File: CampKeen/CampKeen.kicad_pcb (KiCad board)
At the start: 4 copper layers, 177.8 x 142.2 mm, 279 parts, among them IC1 CD74HC4050ME4, IC2 LM2597MX-ADJ_NOPB, IC3 LM2670SX-5.0_NOPB, IC4 DS3231SN#, IC5 OPA2340PA, IC6 OPA2340PA, J1 Vin, J2 Screw_Terminal_01x03, J3 CircuitSetupsSplitPhase, J4 Conn_01x02, J5 Conn_01x02, J6 Conn_01x02, J7 GenEnclosure, J8 GenHeadL, J9 GenHeadR, P1 Power, P10 CONN_01X01, P11 CONN_01X01, P12 CONN_01X01, P13 CONN_01X01, P2 Analog, P3 Analog, P4 Digital, P5 PWM, P6 PWM, P7 Communication, P8 CONN_01X01, P9 CONN_01X01, Q1 IRF9Z34NPBF, Q10 2N7000, Q11 IRF9Z34NPBF, Q12 2N7000, Q13 2N7000, Q14 2N7000, Q15 2N7000, Q16 2N7000, Q17 2N7000, Q18 2N7000, Q19 2N7000, Q2 2N7000, Q20 2N7000, Q21 2N7000, Q22 2N7000, Q23 2N7000, Q24 2N7000, Q25 2N7000, Q26 2N7000, Q27 2N7000, Q28 2N7000, Q29 2N7000, Q3 IRF9Z34NPBF, Q30 2N7000, Q31 2N7000, Q32 IRF9Z34NPBF, Q33 IRF9Z34NPBF, Q34 2N7000, Q35 IRF9Z34NPBF, Q36 2N7000, Q37 IRF9Z34NPBF, Q38 2N7000, Q39 IRF9Z34NPBF, Q4 2N7000, Q40 2N7000, Q41 IRF9Z34NPBF, Q42 2N7000, Q43 2N7000, Q44 IRF9Z34NPBF, Q45 IRF9Z34NPBF, Q46 2N7000, Q47 IRF9Z34NPBF, Q48 2N7000, Q49 IRF9Z34NPBF, Q5 2N7000, Q50 2N7000, Q51 IRF9Z34NPBF, Q52 2N7000, Q53 IRF9Z34NPBF, Q54 2N7000, Q55 IRF9Z34NPBF, Q56 2N7000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

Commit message: some annotation.
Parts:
- removed R117, R120: 10k, Resistor_THT:R_Axial_DIN0207_L6.3mm_D2.5mm_P2.54mm_Vertical
- removed Tanks1, Tanks2: TanksVS, SamacSys_Parts:BK_HTC-15M
- removed Z16, Z17: BZX79C10, SamacSys_Parts:DIOAD1068W53L380D172
- added D4: SR305-TP, SamacSys_Parts:DIOAD2860W130L840D505, F.Cu at (-17.8, -85.2)
- added D5: SR305-TP, SamacSys_Parts:DIOAD2860W130L840D505, F.Cu at (-17.8, -78.3)
- moved Z4 201.9 mm to (-4.99, -48.4)
- moved R81 198.4 mm to (13.5, -25.2)
- moved R112 197.5 mm to (85.7, -66.8)
- moved Q30 190.1 mm to (21.1, -44.5)
- moved R30 188.7 mm to (126.9, -29.9)
- moved Q32 188.5 mm to (10.6, -43.4)
- moved R113 184.6 mm to (85.7, -62.8)
- moved R31 183.6 mm to (120.8, -25.9)
- moved R27 183.0 mm to (126.9, -25.9)
- moved R50 179.8 mm to (61.1, -4.28)
- moved R79 178.8 mm to (25.8, -31.9)
- moved R26 178.2 mm to (126.9, -21.8)
- moved R29 178.2 mm to (120.8, -21.8)
- moved R28 176.1 mm to (114.6, -29.9)
- moved R82 172.2 mm to (25.8, -35.9)
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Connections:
- 5VOut1 pad 1: +5V -> Net-(5VOut1-Pad1)
- 5VOut1 pad 2: Net-(5VOut1-Pad2) -> +5V
- C10 pad 1: +5V -> Net-(5VOut1-Pad1)
- IC3 pad 6: +5V -> Net-(5VOut1-Pad1)
- IO2 pad 1: Net-(5VOut1-Pad2) -> +5V
- J2 pad 1: +12V -> Net-(D4-Pad1)
- L1 pad 2: +5V -> Net-(5VOut1-Pad1)
- Q11 pad 3: Net-(Q11-Pad3) -> +BATT
- Q16 pad 3: +5V -> +5VL
- Q17 pad 3: +5V -> +5VL
- Q18 pad 3: +5V -> +5VL
- Q19 pad 3: +5V -> +5VL
- Q20 pad 3: +5V -> +5VL
- Q21 pad 3: +5V -> +5VL
- Q22 pad 3: +5V -> +5VL
- Q23 pad 3: +5V -> +5VL
- Q24 pad 3: +5V -> +5VL
- Q25 pad 3: +5V -> +5VL
- Q26 pad 3: +5V -> +5VL
- Q27 pad 3: +5V -> +5VL
- Q28 pad 3: +5V -> +5VL
- Q29 pad 3: +5V -> +5VL
- Q3 pad 3: Net-(Q3-Pad3) -> +BATT
- Q55 pad 1: Net-(Q55-Pad1) -> Net-(Q54-Pad3)
- Q57 pad 1: Net-(Q57-Pad1) -> Net-(Q56-Pad3)
- R116 pad 2: Net-(Q55-Pad1) -> Net-(Q54-Pad3)
- R119 pad 2: Net-(Q57-Pad1) -> Net-(Q56-Pad3)
- R16 pad 1: Net-(Q3-Pad3) -> +BATT
- R41 pad 1: Net-(Q11-Pad3) -> +BATT
- Z1 pad 1: Net-(Q3-Pad3) -> +BATT
- Z3 pad 1: Net-(Q11-Pad3) -> +BATT
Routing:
- net Net-(D2-Pad1): track 20.6 -> 5.43 mm
- net Net-(5VOut1-Pad1): track 0.00 -> 13.9 mm
- net +5V: track 14.0 -> 0.10 mm

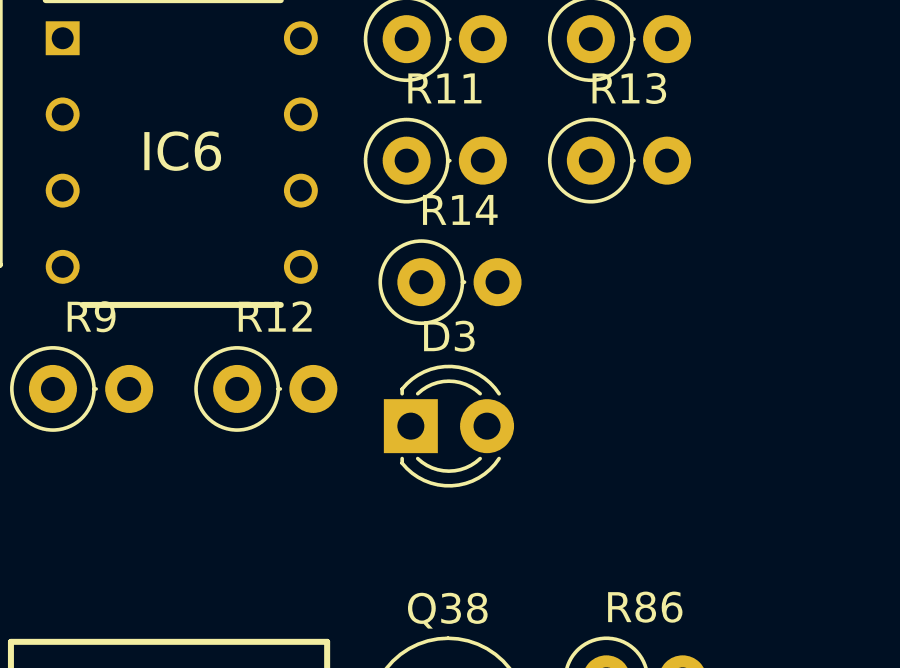
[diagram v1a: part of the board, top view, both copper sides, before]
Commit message: added ACEMON on boot and Waterpumpsense on boot commands. Autoformat
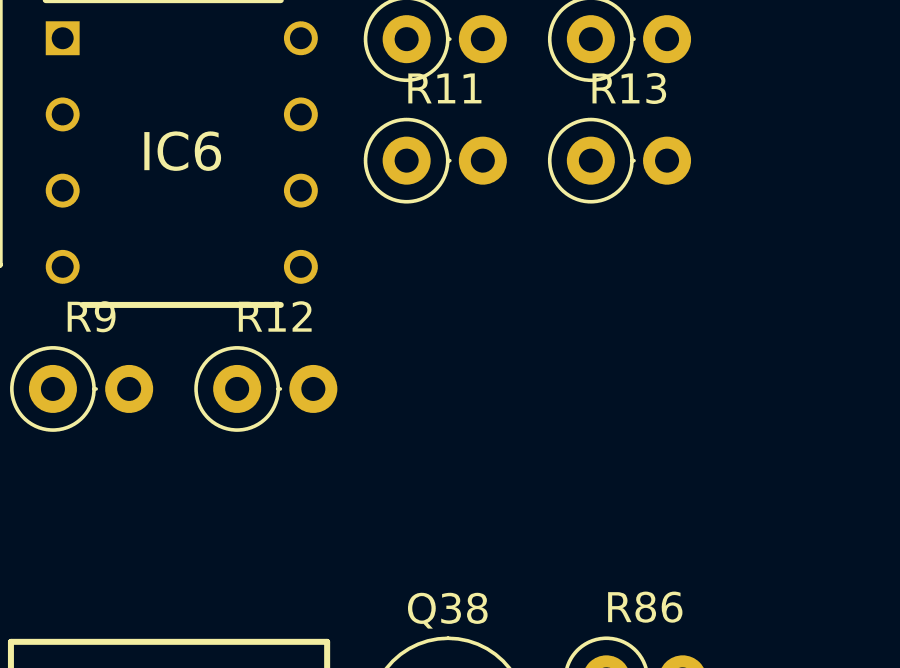
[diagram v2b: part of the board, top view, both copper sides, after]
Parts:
- removed D3: LED, LED_THT:LED_D3.0mm
- removed R14: 330, Resistor_THT:R_Axial_DIN0207_L6.3mm_D2.5mm_P2.54mm_Vertical
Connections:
- P5 pad 5: DisplayLED -> (no net)

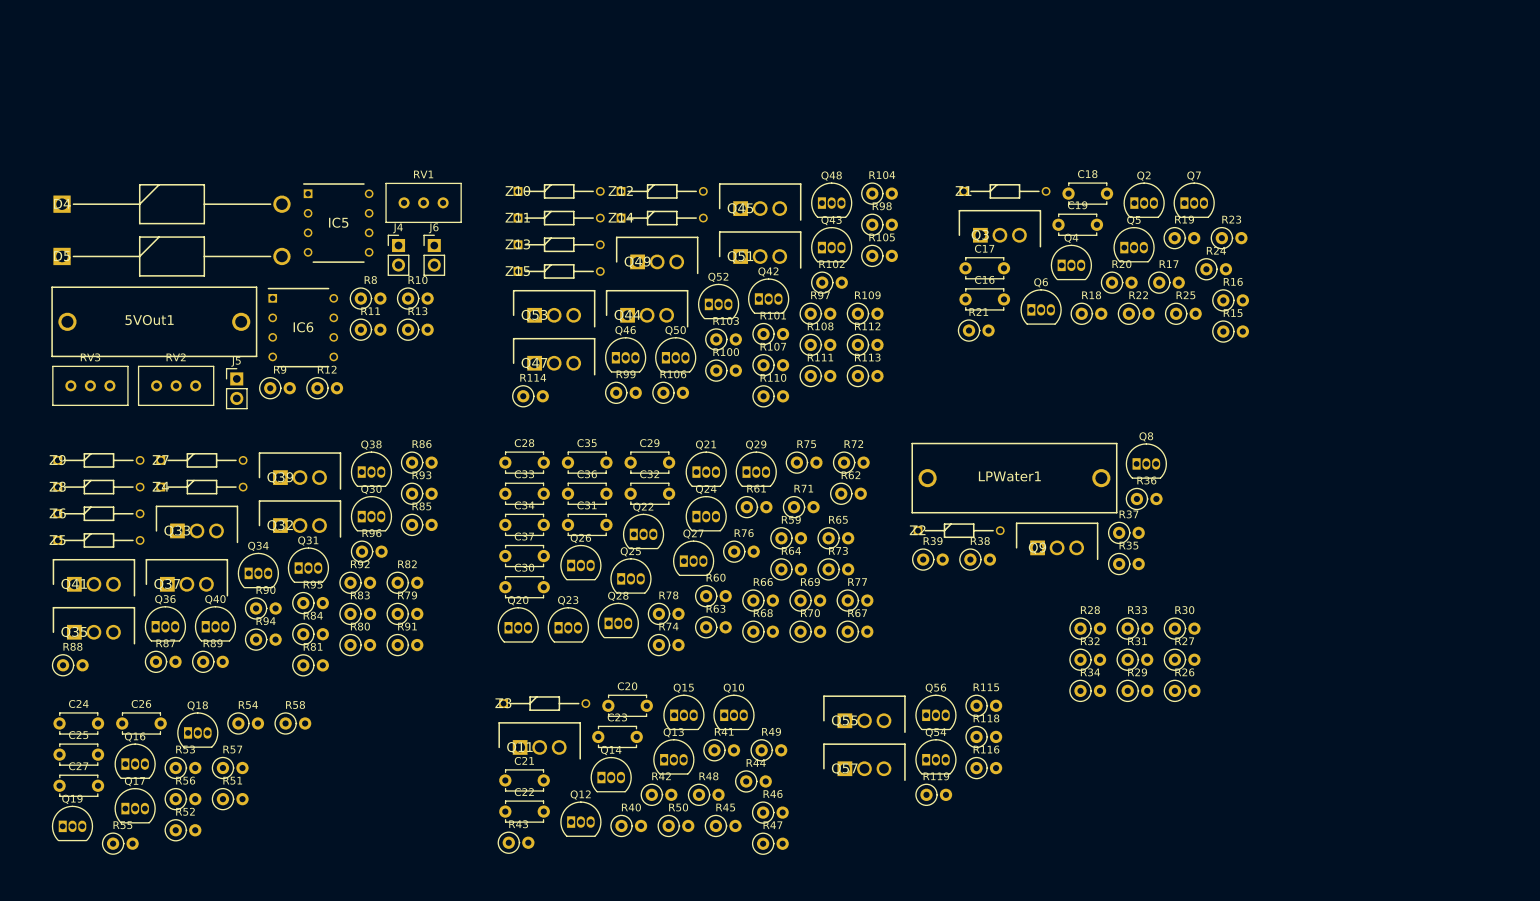
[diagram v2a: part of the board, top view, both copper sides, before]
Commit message: schematic done for Input isolation updates.
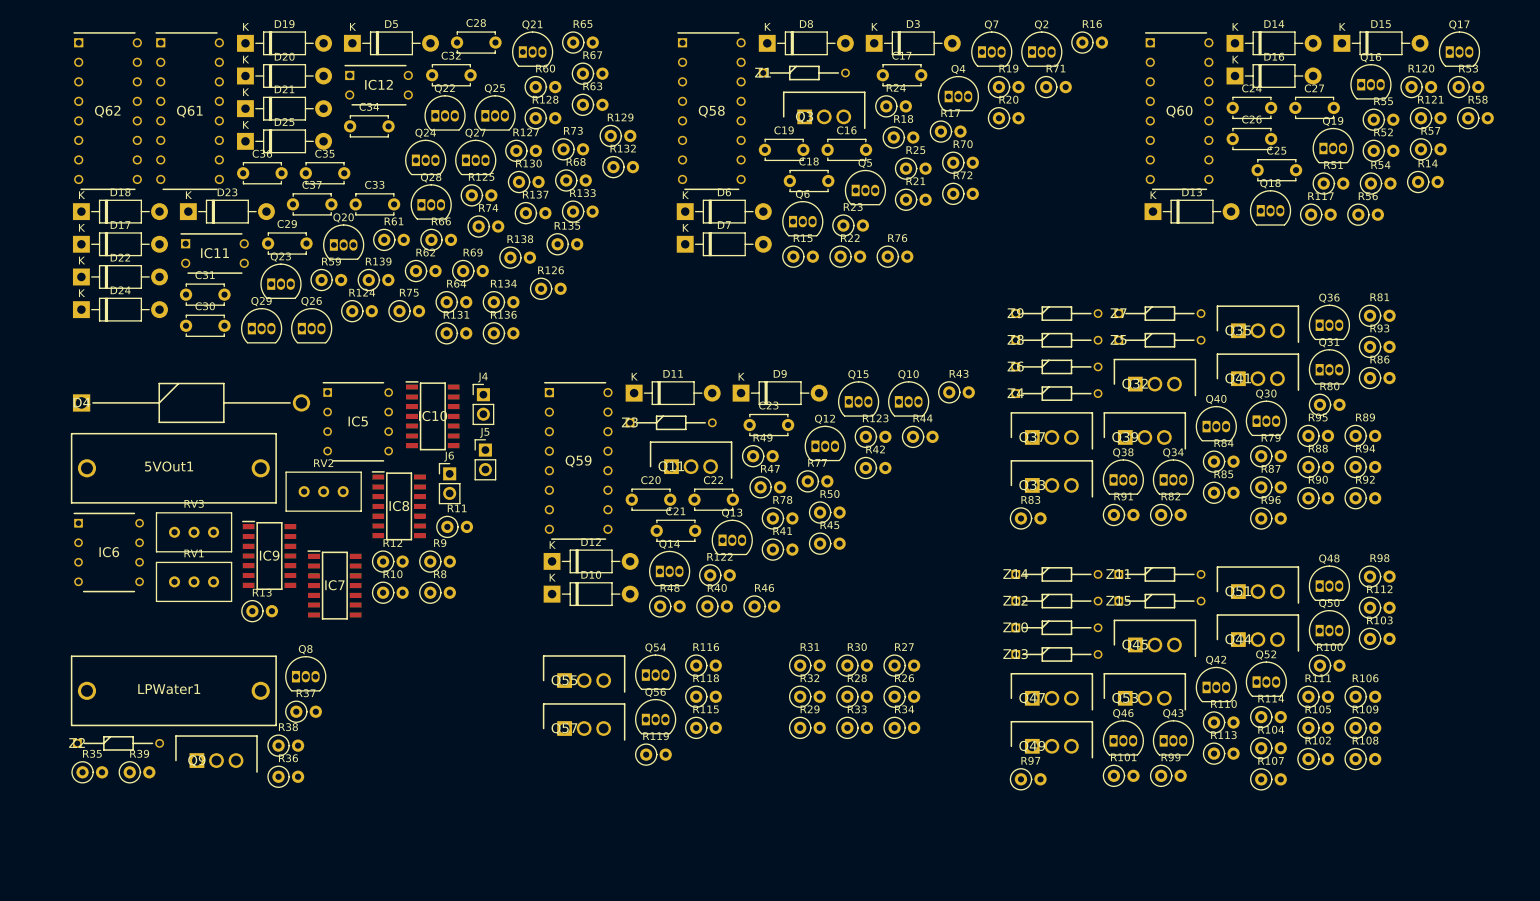
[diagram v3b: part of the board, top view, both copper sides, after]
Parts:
- added D10: 1N4007, Diode_THT:D_DO-41_SOD81_P10.16mm_Horizontal, F.Cu at (45.9, -34.4)
- added D11: 1N4007, Diode_THT:D_DO-41_SOD81_P10.16mm_Horizontal, F.Cu at (56.6, -60.6)
- added D12: 1N4007, Diode_THT:D_DO-41_SOD81_P10.16mm_Horizontal, F.Cu at (45.9, -38.7)
- added D13: 1N4007, Diode_THT:D_DO-41_SOD81_P10.16mm_Horizontal, F.Cu at (124.1, -84.2)
- added D14: 1N4007, Diode_THT:D_DO-41_SOD81_P10.16mm_Horizontal, F.Cu at (134.7, -106.1)
- added D15: 1N4007, Diode_THT:D_DO-41_SOD81_P10.16mm_Horizontal, F.Cu at (148.6, -106.1)
- added D16: 1N4007, Diode_THT:D_DO-41_SOD81_P10.16mm_Horizontal, F.Cu at (134.7, -101.8)
- added D17: 1N4007, Diode_THT:D_DO-41_SOD81_P10.16mm_Horizontal, F.Cu at (-15.3, -79.9)
- added D18: 1N4007, Diode_THT:D_DO-41_SOD81_P10.16mm_Horizontal, F.Cu at (-15.3, -84.2)
- added D19: 1N4007, Diode_THT:D_DO-41_SOD81_P10.16mm_Horizontal, F.Cu at (6.01, -106.1)
- added D20: 1N4007, Diode_THT:D_DO-41_SOD81_P10.16mm_Horizontal, F.Cu at (6.01, -101.8)
- added D21: 1N4007, Diode_THT:D_DO-41_SOD81_P10.16mm_Horizontal, F.Cu at (6.01, -97.6)
- added D22: 1N4007, Diode_THT:D_DO-41_SOD81_P10.16mm_Horizontal, F.Cu at (-15.3, -75.7)
- added D23: 1N4007, Diode_THT:D_DO-41_SOD81_P10.16mm_Horizontal, F.Cu at (-1.42, -84.2)
- added D24: 1N4007, Diode_THT:D_DO-41_SOD81_P10.16mm_Horizontal, F.Cu at (-15.3, -71.4)
- added D25: 1N4007, Diode_THT:D_DO-41_SOD81_P10.16mm_Horizontal, F.Cu at (6.01, -93.3)
- added D3: 1N4007, Diode_THT:D_DO-41_SOD81_P10.16mm_Horizontal, F.Cu at (87.8, -106.1)
- added D6: 1N4007, Diode_THT:D_DO-41_SOD81_P10.16mm_Horizontal, F.Cu at (63.2, -84.2)
- added D7: 1N4007, Diode_THT:D_DO-41_SOD81_P10.16mm_Horizontal, F.Cu at (63.2, -79.9)
- added D8: 1N4007, Diode_THT:D_DO-41_SOD81_P10.16mm_Horizontal, F.Cu at (73.9, -106.1)
- added D9: 1N4007, Diode_THT:D_DO-41_SOD81_P10.16mm_Horizontal, F.Cu at (70.5, -60.6)
- added IC10: SN7404DR, SamacSys_Parts:SOIC127P600X175-14N, F.Cu at (30.4, -57.5)
- added IC11: LTV-814, SamacSys_Parts:DIP762W60P254L460H450Q4N, F.Cu at (2.04, -78.7)
- added IC12: LTV-814, SamacSys_Parts:DIP762W60P254L460H450Q4N, F.Cu at (23.4, -100.6)
- added IC7: SN7404DR, SamacSys_Parts:SOIC127P600X175-14N, F.Cu at (17.6, -35.5)
- added IC8: SN7404DR, SamacSys_Parts:SOIC127P600X175-14N, F.Cu at (26.0, -45.8)
- added IC9: SN7404DR, SamacSys_Parts:SOIC127P600X175-14N, F.Cu at (9.14, -39.4)
- added Q58: LTV-847, SamacSys_Parts:DIP762W60P254L1984H450Q16N, F.Cu at (66.7, -97.3)
- added Q59: LTV-847, SamacSys_Parts:DIP762W60P254L1984H450Q16N, F.Cu at (49.4, -51.8)
- added Q60: LTV-847, SamacSys_Parts:DIP762W60P254L1984H450Q16N, F.Cu at (127.5, -97.3)
- added Q61: LTV-847, SamacSys_Parts:DIP762W60P254L1984H450Q16N, F.Cu at (-1.20, -97.3)
- added Q62: LTV-847, SamacSys_Parts:DIP762W60P254L1984H450Q16N, F.Cu at (-11.9, -97.3)
- added R117: 330, Resistor_THT:R_Axial_DIN0207_L6.3mm_D2.5mm_P2.54mm_Vertical, F.Cu at (144.6, -83.8)
- added R120: 330, Resistor_THT:R_Axial_DIN0207_L6.3mm_D2.5mm_P2.54mm_Vertical, F.Cu at (157.7, -100.4)
- added R121: 330, Resistor_THT:R_Axial_DIN0207_L6.3mm_D2.5mm_P2.54mm_Vertical, F.Cu at (158.9, -96.3)
- added R122: 22k, Resistor_THT:R_Axial_DIN0207_L6.3mm_D2.5mm_P2.54mm_Vertical, F.Cu at (66.5, -36.9)
- added R123: 22k, Resistor_THT:R_Axial_DIN0207_L6.3mm_D2.5mm_P2.54mm_Vertical, F.Cu at (86.7, -54.9)
- added R124: 330, Resistor_THT:R_Axial_DIN0207_L6.3mm_D2.5mm_P2.54mm_Vertical, F.Cu at (19.9, -71.2)
- added R125: 22k, Resistor_THT:R_Axial_DIN0207_L6.3mm_D2.5mm_P2.54mm_Vertical, F.Cu at (35.5, -86.3)
- added R126: 330, Resistor_THT:R_Axial_DIN0207_L6.3mm_D2.5mm_P2.54mm_Vertical, F.Cu at (44.5, -74.1)
- added R127: 22k, Resistor_THT:R_Axial_DIN0207_L6.3mm_D2.5mm_P2.54mm_Vertical, F.Cu at (41.2, -92.1)
- added R128: 22k, Resistor_THT:R_Axial_DIN0207_L6.3mm_D2.5mm_P2.54mm_Vertical, F.Cu at (43.8, -96.3)
- added R129: 22k, Resistor_THT:R_Axial_DIN0207_L6.3mm_D2.5mm_P2.54mm_Vertical, F.Cu at (53.5, -94.0)
- added R130: 22k, Resistor_THT:R_Axial_DIN0207_L6.3mm_D2.5mm_P2.54mm_Vertical, F.Cu at (41.6, -88.0)
- added R131: 22k, Resistor_THT:R_Axial_DIN0207_L6.3mm_D2.5mm_P2.54mm_Vertical, F.Cu at (32.2, -68.4)
- added R132: 330, Resistor_THT:R_Axial_DIN0207_L6.3mm_D2.5mm_P2.54mm_Vertical, F.Cu at (53.9, -90.0)
- added R133: 300, Resistor_THT:R_Axial_DIN0207_L6.3mm_D2.5mm_P2.54mm_Vertical, F.Cu at (48.6, -84.2)
- added R134: 330, Resistor_THT:R_Axial_DIN0207_L6.3mm_D2.5mm_P2.54mm_Vertical, F.Cu at (38.3, -72.4)
- added R135: 330, Resistor_THT:R_Axial_DIN0207_L6.3mm_D2.5mm_P2.54mm_Vertical, F.Cu at (46.6, -79.9)
- added R136: 22k, Resistor_THT:R_Axial_DIN0207_L6.3mm_D2.5mm_P2.54mm_Vertical, F.Cu at (38.3, -68.4)
- added R137: 22k, Resistor_THT:R_Axial_DIN0207_L6.3mm_D2.5mm_P2.54mm_Vertical, F.Cu at (42.5, -84.0)
- added R138: 22k, Resistor_THT:R_Axial_DIN0207_L6.3mm_D2.5mm_P2.54mm_Vertical, F.Cu at (40.5, -78.2)
- added R139: 22k, Resistor_THT:R_Axial_DIN0207_L6.3mm_D2.5mm_P2.54mm_Vertical, F.Cu at (22.1, -75.3)
- added R14: 330, Resistor_THT:R_Axial_DIN0207_L6.3mm_D2.5mm_P2.54mm_Vertical, F.Cu at (158.5, -88.0)
- D5: value SR305-TP -> 1N4007; footprint SamacSys_Parts:DIOAD2860W130L840D505 -> Diode_THT:D_DO-41_SOD81_P10.16mm_Horizontal
- R20, R21, R24, R25, R45, R46, R49, R50, R63, R64, R66: value 1M -> 330
- R53, R54, R57, R58, R70, R71, R72, R76, R77, R78: value 1M -> 22k
- R65: value 1M -> 300
- moved Q17 198.4 mm to (162.7, -104.9)
- moved R55 189.1 mm to (152.8, -96.1)
- moved R53 188.9 mm to (163.8, -100.4)
- moved Q19 186.2 mm to (146.2, -92.4)
- moved Q16 183.4 mm to (151.1, -100.7)
- moved C27 183.3 mm to (142.6, -97.7)
- moved R52 179.1 mm to (152.8, -92.1)
- moved R57 175.4 mm to (158.9, -92.3)
- moved C25 173.4 mm to (137.7, -89.6)
- moved R58 172.8 mm to (165.1, -96.3)
- moved C24 172.3 mm to (134.4, -97.7)
- moved R56 171.6 mm to (150.8, -83.8)
- moved R51 164.0 mm to (146.3, -87.8)
- moved R88 164.0 mm to (144.3, -51.0)
- moved C26 163.2 mm to (134.4, -93.6)
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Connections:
- D5 pad 1: +5VL -> Net-(D5-Pad1)
- D5 pad 2: +5V -> Net-(D5-Pad2)
- Q12 pad 1: G1-4 -> GND
- Q12 pad 3: +5V -> Net-(D9-Pad1)
- Q13 pad 1: G1-2 -> GND
- Q13 pad 3: +5V -> Net-(D10-Pad1)
- Q14 pad 1: G4-4 -> GND
- Q14 pad 3: +5V -> Net-(D12-Pad1)
- Q15 pad 1: G3-4 -> GND
- Q15 pad 3: +5V -> Net-(D11-Pad1)
- Q16 pad 1: AlarmTTL -> GND
- Q16 pad 3: +5VL -> Net-(D13-Pad1)
- Q17 pad 1: KitchenTTL -> GND
- Q17 pad 3: +5VL -> Net-(D16-Pad1)
- Q18 pad 1: SpareTTL -> GND
- Q18 pad 3: +5VL -> Net-(D14-Pad1)
- Q19 pad 1: BathRoomTTL -> GND
- Q19 pad 3: +5VL -> Net-(D15-Pad1)
- Q20 pad 1: WPS -> GND
- Q20 pad 3: +5VL -> Net-(D5-Pad1)
- Q21 pad 1: ENLCD -> GND
- Q21 pad 3: +5VL -> Net-(D17-Pad1)
- Q22 pad 1: LCBBACK -> GND
- Q22 pad 3: +5VL -> Net-(D18-Pad1)
- Q23 pad 1: WSS -> GND
- Q23 pad 3: +5VL -> Net-(D19-Pad1)
- Q24 pad 1: SPIn1 -> GND
- Q24 pad 3: +5VL -> Net-(D22-Pad1)
- Q25 pad 1: SPIn3 -> GND
- Q25 pad 3: +5VL -> Net-(D24-Pad1)
- Q26 pad 1: SPIn5 -> GND
- Q26 pad 3: +5VL -> Net-(D20-Pad1)
- Q27 pad 1: SPIn6 -> GND
- Q27 pad 3: +5VL -> Net-(D21-Pad1)
- Q28 pad 1: SPIn2 -> GND
- Q28 pad 3: +5VL -> Net-(D23-Pad1)
- Q29 pad 1: SPIn4 -> GND
- Q29 pad 3: +5VL -> Net-(D25-Pad1)
- Q4 pad 1: S1-4 -> GND
- Q4 pad 3: +5V -> Net-(D3-Pad1)
- Q5 pad 1: S1-2 -> GND
- Q5 pad 3: +5V -> Net-(D6-Pad1)
- Q6 pad 1: S4-4 -> GND
- Q6 pad 3: +5V -> Net-(D8-Pad1)
- Q7 pad 1: S3-4 -> GND
- Q7 pad 3: +5V -> Net-(D7-Pad1)
- R20 pad 1: S1-4 -> +5V
- R20 pad 2: GND -> Net-(Q58-Pad7)
- R21 pad 1: S1-2 -> +5V
- R21 pad 2: GND -> Net-(Q58-Pad1)
- R24 pad 1: S4-4 -> +5V
- R24 pad 2: GND -> Net-(Q58-Pad5)
- R25 pad 1: S3-4 -> +5V
- R25 pad 2: GND -> Net-(Q58-Pad3)
- R45 pad 1: G1-4 -> +5V
- R45 pad 2: GND -> Net-(Q59-Pad7)
- R46 pad 1: G1-2 -> +5V
- R46 pad 2: GND -> Net-(Q59-Pad1)
- R49 pad 1: G4-4 -> +5V
- R49 pad 2: GND -> Net-(Q59-Pad5)
- R50 pad 1: G3-4 -> +5V
- R50 pad 2: GND -> Net-(Q59-Pad3)
- R53 pad 1: AlarmTTL -> +5V
- R53 pad 2: GND -> /Inputs With Interrupts/AlarmResetTTL
- R54 pad 1: KitchenTTL -> +5V
- R54 pad 2: GND -> /Inputs With Interrupts/KitchenTTL
- R57 pad 1: SpareTTL -> +5V
- R57 pad 2: GND -> /Inputs With Interrupts/SpareInterruptTTL
- R58 pad 1: BathRoomTTL -> +5V
- R58 pad 2: GND -> /Inputs With Interrupts/BathroomTTL
- R63 pad 1: WPS -> +5V
- R63 pad 2: GND -> Net-(Q61-Pad3)
- R64 pad 1: ENLCD -> +5V
- R64 pad 2: GND -> Net-(Q61-Pad1)
- R65 pad 1: LCBBACK -> +5V
- R65 pad 2: GND -> Net-(Q61-Pad5)
- R66 pad 1: WSS -> +5V
- R66 pad 2: GND -> Net-(Q61-Pad7)
- R70 pad 1: SPIn1 -> +5V
- R70 pad 2: GND -> /Tanks/1-4OUT
- R71 pad 1: SPIn3 -> +5V
- R71 pad 2: GND -> /Tanks/1-2OUT
- R72 pad 1: SPIn5 -> +5V
- R72 pad 2: GND -> /Tanks/3-4OUT
- R76 pad 1: SPIn6 -> +5V
- R76 pad 2: GND -> /Tanks/FullOUT
- R77 pad 1: SPIn2 -> +5V
- R77 pad 2: GND -> /sheet6479D10C/1-4OUT
- R78 pad 1: SPIn4 -> +5V
- R78 pad 2: GND -> /sheet6479D10C/1-2OUT

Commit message: wip for PCB Layout
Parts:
- moved D3 364.5 mm to (229.1, 229.9), turned to 180 degrees
- moved D8 358.6 mm to (229.1, 217.2), turned to 180 degrees
- moved Q4 356.8 mm to (235.5, 229.9), turned to 180 degrees
- moved R18 355.2 mm to (239.3, 228.6), turned to 270 degrees
- moved Q58 350.7 mm to (211.3, 222.2), turned to 180 degrees
- moved R19 349.8 mm to (239.3, 222.2), turned to 270 degrees
- moved D6 349.6 mm to (229.1, 223.5), turned to 180 degrees
- moved Q5 344.8 mm to (235.5, 223.5), turned to 180 degrees
- moved R24 343.5 mm to (192.3, 229.9), turned to 270 degrees
- moved Q7 342.9 mm to (235.5, 210.8), turned to 180 degrees
- moved R20 341.9 mm to (202.4, 231.1)
- moved C7 340.0 mm to (-208.7, 85.0)
- moved D1 340.0 mm to (-213.8, 85.0)
- moved Q6 339.2 mm to (235.5, 217.2), turned to 180 degrees
- moved C10 338.8 mm to (-222.7, 68.5)
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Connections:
- P5 pad 1: SCL -> (no net)
- P5 pad 2: SDA -> (no net)
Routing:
- net GND: track 216.4 -> 0.00 mm, vias 1 -> 0
- net +9V: track 82.3 -> 0.00 mm
- net +12V: track 50.4 -> 0.00 mm, vias 1 -> 0
- net KLED: track 39.2 -> 0.00 mm, vias 1 -> 0
- net Net-(C7-Pad2): track 31.7 -> 0.00 mm
- net Net-(C2-Pad1): track 31.0 -> 0.00 mm
- net Net-(C1-Pad1): track 27.7 -> 0.00 mm
- net Net-(C7-Pad1): track 18.2 -> 0.00 mm, vias 1 -> 0
- net Net-(C8-Pad1): track 16.1 -> 0.00 mm
- net Net-(5VOut1-Pad1): track 13.9 -> 0.00 mm
- net Net-(IC3-Pad5): track 6.18 -> 0.00 mm
- net Net-(D2-Pad1): track 5.43 -> 0.00 mm
- net Net-(IC2-Pad1): track 5.17 -> 0.00 mm
- removed copper zone on B.Cu, net GND
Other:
- board text added: "+5V MAX RTC"
- board text added: "- RTC"
- board text added: "Grey Tank"
- board text added: "RS232"
- board text added: "Sewage Tank"
- board text removed: "5V Power"
- board text removed: "9V Power"

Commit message: continuing WIP for PCB layout.
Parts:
- moved C6 376.5 mm to (149.1, 106.7), turned to 270 degrees
- moved C5 373.2 mm to (150.4, 97.8), turned to 270 degrees
- moved C4 364.8 mm to (142.7, 98.1), turned to 270 degrees
- moved D4 364.7 mm to (168.1, 109.2), turned to 270 degrees
- moved C10 357.8 mm to (133.9, 99.1), turned to 270 degrees
- moved IC3 350.5 mm to (137.7, 111.8), turned to 180 degrees
- moved R4 333.3 mm to (122.5, 109.6), turned to 270 degrees
- moved L1 330.7 mm to (116.1, 101.6), turned to 270 degrees
- moved D1 322.9 mm to (108.5, 105.4), turned to 90 degrees
- moved C7 317.0 mm to (107.2, 111.8), turned to 270 degrees
- moved C24 307.2 mm to (312.2, 158.9)
- moved C25 307.2 mm to (315.5, 167.0)
- moved C26 307.2 mm to (312.2, 162.9)
- moved C27 307.2 mm to (320.4, 158.9)
- moved R117 307.2 mm to (322.4, 172.8)
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
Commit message: upgrade to kicad 6.0
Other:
- net class Default removed

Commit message: wip for PCB layout.
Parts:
- moved R120 93.6 mm to (281.3, 232.5), turned to 90 degrees
- moved R58 92.0 mm to (269.1, 215.3)
- moved R14 91.4 mm to (271.0, 232.5), turned to 90 degrees
- moved R53 90.7 mm to (269.1, 210.6)
- moved R121 88.1 mm to (286.3, 232.5), turned to 90 degrees
- moved R57 86.6 mm to (269.2, 218.5), turned to -90 degrees
- moved R54 82.4 mm to (269.2, 224.1), turned to -90 degrees
- moved R117 75.5 mm to (276.3, 232.5), turned to 90 degrees
- moved R55 69.7 mm to (275.0, 202.5), turned to 90 degrees
- moved Q60 66.4 mm to (283.1, 222.5), turned to 90 degrees
- moved R51 62.0 mm to (270.0, 199.0)
- moved C20 57.2 mm to (255.2, 205.3)
- moved C24 56.5 mm to (268.3, 194.4)
- moved D15 53.7 mm to (285.8, 206.2)
- moved D16 53.7 mm to (290.9, 206.2)
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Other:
- board size 177.8 x 142.2 mm -> 193.7 x 142.2 mm

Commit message: wip for Placement on PCB
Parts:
- moved D19 484.8 mm to (269.9, 188.1)
- moved Q61 483.5 mm to (287.4, 177.7)
- moved D18 475.5 mm to (269.9, 183.2)
- moved Q62 473.7 mm to (287.4, 156.6)
- moved D17 468.4 mm to (269.9, 178.5)
- moved D5 465.0 mm to (269.9, 173.5)
- moved D25 458.2 mm to (269.9, 168.5)
- moved D24 450.2 mm to (269.9, 163.5)
- moved D23 447.6 mm to (269.9, 158.7)
- moved C31 446.5 mm to (257.6, 177.2), turned to -90 degrees
- moved D22 446.1 mm to (269.9, 153.9)
- moved C36 440.8 mm to (242.6, 170.1), turned to -90 degrees
- moved C37 439.8 mm to (242.6, 177.2), turned to -90 degrees
- moved Q22 439.8 mm to (247.2, 174.1)
- moved Q23 438.4 mm to (247.2, 180.9)
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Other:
- outline, holes or cut-outs redrawn
